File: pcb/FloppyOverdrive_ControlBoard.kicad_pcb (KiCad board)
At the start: 2 copper layers, 163 x 104 mm, 78 parts, among them IC1 THS4521IDR, IC2 THS4521IDR, IC3 MAX660MX_NOPB, J1 174804-1, J10 Flop_ADC_Header, J2 Motor_Header, J3 Floppy_Bus, J4 Sensor_Header, J5 Heads_Header, J6 Step_Header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

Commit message: Fixed pin 39, added missing hole to PCB
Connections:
- J8 pad 39: +3.3V -> +3V3
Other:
- outline, holes or cut-outs redrawn
- board text added: "+3.3V"
- board text added: "+5V"
- board text added: "2x 47uF"
- board text added: "Floppy Bus"
- board text added: "GND"
- board text added: "Replaces Mitsubishi NAMFN motherboard for MF504A"
- board text removed: "Replaces Mitsubishi NAMFN motherboard"

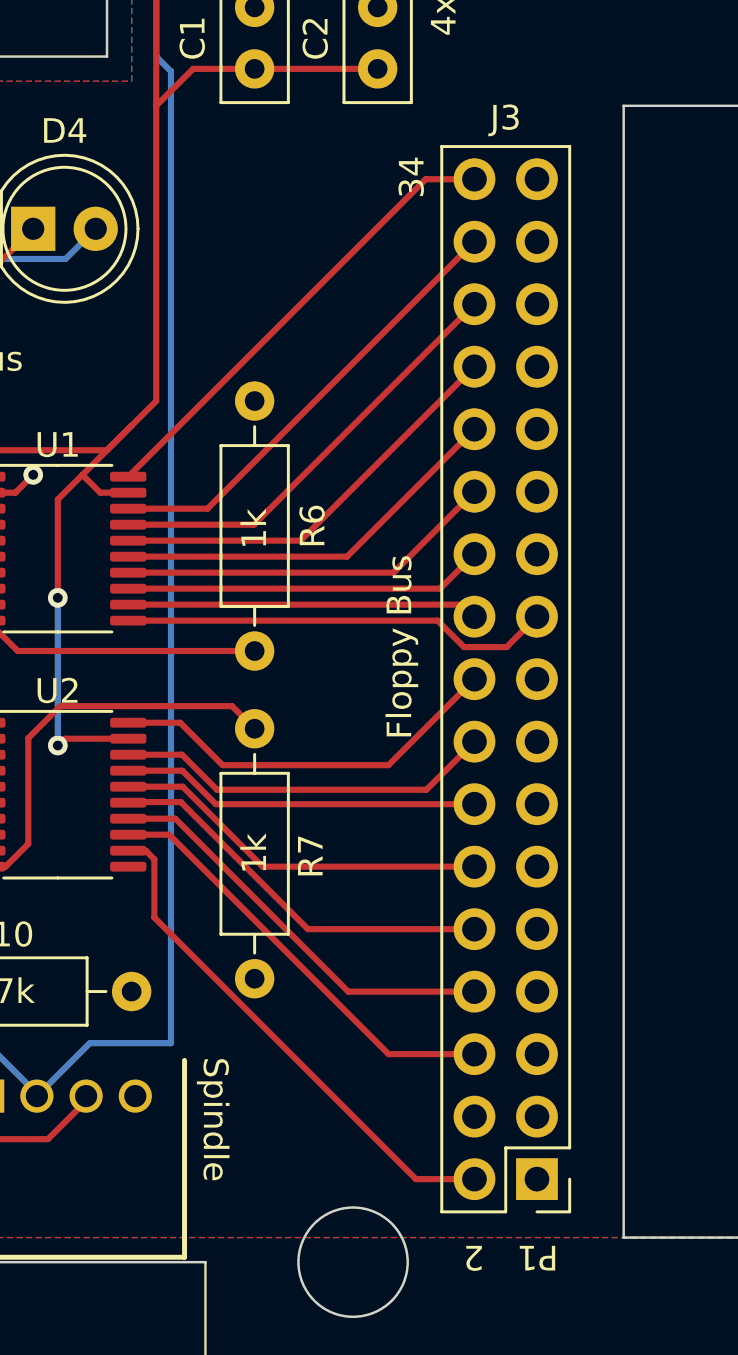
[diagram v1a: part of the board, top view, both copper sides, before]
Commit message: Added bus pinout to silkscreen
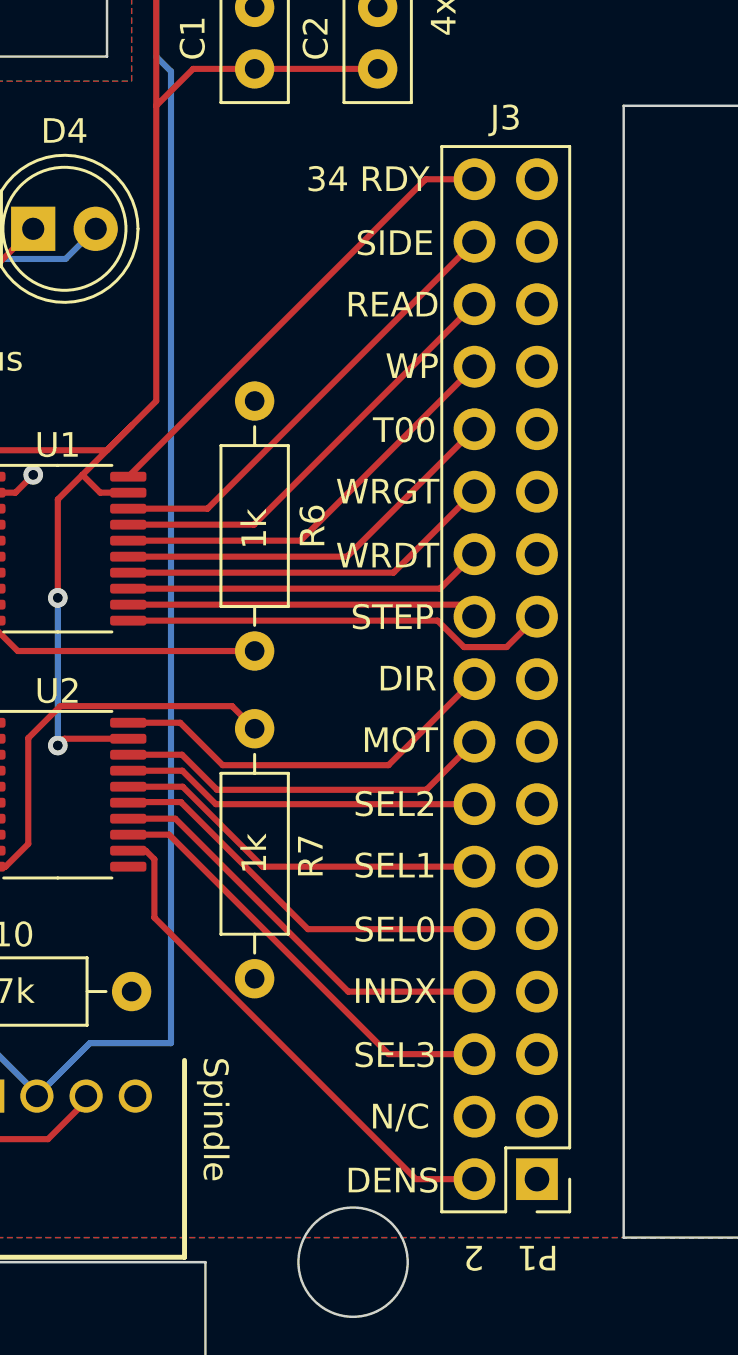
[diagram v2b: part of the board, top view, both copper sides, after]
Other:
- board text added: "34 RDY"
- board text added: "DENS"
- board text added: "DIR"
- board text added: "INDX"
- board text added: "MOT"
- board text added: "N/C"
- board text added: "READ"
- board text added: "SEL0"
- board text added: "SEL1"
- board text added: "SEL2"
- board text added: "SEL3"
- board text added: "SIDE"
- board text added: "STEP"
- board text added: "T00"
- board text added: "WRDT"
- board text added: "WRGT"
- board text removed: "34"
- board text removed: "Floppy Bus"
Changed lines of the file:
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@@
+    (effects (font (size 1 1) (thickness 0.15)))
+  )
+  (gr_text "N/C" (at 210.9 135.1) (layer "F.SilkS")
     (effects (font (size 1 1) (thickness 0.15)))
   )
@@
     (effects (font (size 1 1) (thickness 0.15)))
   )
+  (gr_text "WP" (at 211.4 104.6) (layer "F.SilkS")
+    (effects (font (size 1 1) (thickness 0.15)))
+  )
   (gr_text "Head 0      1" (at 98 98.8) (layer "F.SilkS")
     (effects (font (size 1 1) (thickness 0.15)))
   )
   (gr_text "Side A\nSide B" (at 77 118 270) (layer "F.SilkS")
+    (effects (font (size 1 1) (thickness 0.15)))
+  )
+  (gr_text "SEL1" (at 210.7 124.9) (layer "F.SilkS")
     (effects (font (size 1 1) (thickness 0.15)))
   )
@@
     (effects (font (size 0.75 0.75) (thickness 0.1)))
   )
+  (gr_text "SEL3" (at 210.7 132.6) (layer "F.SilkS")
+    (effects (font (size 1 1) (thickness 0.15)))
+  )
   (gr_text "ADC Pins" (at 154 134.2) (layer "F.SilkS")
     (effects (font (size 1 1) (thickness 0.15)))
@@
     (effects (font (size 1 1) (thickness 0.15)))
   )
+  (gr_text "INDX" (at 210.7 130) (layer "F.SilkS")
+    (effects (font (size 1 1) (thickness 0.15)))
+  )
   (gr_text "22k" (at 101.7 142.24) (layer "F.SilkS")
     (effects (font (size 1 1) (thickness 0.15)))
@@
     (effects (font (size 1 1) (thickness 0.15)))
   )
-  (gr_text "Floppy Bus" (at 210.9 116 90) (layer "F.SilkS")
+  (gr_text "DENS" (at 210.6 137.7) (layer "F.SilkS")
     (effects (font (size 1 1) (thickness 0.15)))
   )
@@
     (effects (font (size 1 1) (thickness 0.15)))
   )
+  (gr_text "MOT" (at 210.9 119.8) (layer "F.SilkS")
+    (effects (font (size 1 1) (thickness 0.15)))
+  )
+  (gr_text "WRGT" (at 210.4 109.7) (layer "F.SilkS")
+    (effects (font (size 1 1) (thickness 0.15)))
+  )
   (gr_text "ULN2003C" (at 182 121.3) (layer "F.SilkS")
     (effects (font (size 1 1) (thickness 0.15)))
   )
+  (gr_text "SIDE" (at 210.7 99.6) (layer "F.SilkS")
+    (effects (font (size 1 1) (thickness 0.15)))
+  )
+  (gr_text "READ" (at 210.6 102.1) (layer "F.SilkS")
+    (effects (font (size 1 1) (thickness 0.15)))
+  )
   (gr_text "4-Pin Power" (at 223.2 63.8 90) (layer "F.SilkS")
     (effects (font (size 1 1) (thickness 0.15)))
   )
+  (gr_text "34 RDY" (at 209.6 97) (layer "F.SilkS")
+    (effects (font (size 1 1) (thickness 0.15)))
+  )
   (gr_text "2x 33uF Electrolytic" (at 212 68 270) (layer "F.SilkS")
     (effects (font (size 1 1) (thickness 0.15)))
@@
     (effects (font (size 1 1) (thickness 0.15)))
   )
+  (gr_text "STEP" (at 210.6 114.8) (layer "F.SilkS")
+    (effects (font (size 1 1) (thickness 0.15)))
+  )
   (gr_text "0.1uF" (at 163 127.8 90) (layer "F.SilkS")
     (effects (font (size 1 1) (thickness 0.15)))
   )
+  (gr_text "SEL2" (at 210.7 122.4) (layer "F.SilkS")
+    (effects (font (size 1 1) (thickness 0.15)))
+  )
   (gr_text "+" (at 93.7 101.1) (layer "F.SilkS")
     (effects (font (size 1 1) (thickness 0.15)))
@@
     (effects (font (size 1 1) (thickness 0.15)))
   )
+  (gr_text "WRDT" (at 210.4 112.3) (layer "F.SilkS")
+    (effects (font (size 1 1) (thickness 0.15)))
+  )
+  (gr_text "SEL0" (at 210.7 127.5) (layer "F.SilkS")
+    (effects (font (size 1 1) (thickness 0.15)))
+  )
   (gr_text "510" (at 158.75 99.985 90) (layer "F.SilkS")
     (effects (font (size 1 1) (thickness 0.15)))
   )
+  (gr_text "T00" (at 211.1 107.2) (layer "F.SilkS")
+    (effects (font (size 1 1) (thickness 0.15)))
+  )
   (gr_text "1k" (at 142.75 101 90) (layer "F.SilkS")
     (effects (font (size 1 1) (thickness 0.15)))
@@
     (effects (font (size 1 1) (thickness 0.15)))
   )
+  (gr_text "DIR" (at 211.2 117.3) (layer "F.SilkS")
+    (effects (font (size 1 1) (thickness 0.15)))
+  )
   (gr_text "2x 47uF" (at 109.1 106) (layer "F.SilkS")
     (effects (font (size 1 1) (thickness 0.15)))
@@
     (effects (font (size 1 1) (thickness 0.15)))
   )
-  (gr_text "34" (at 211.4 96.9 90) (layer "F.SilkS")
-    (effects (font (size 1 1) (thickness 0.15)))
-  )

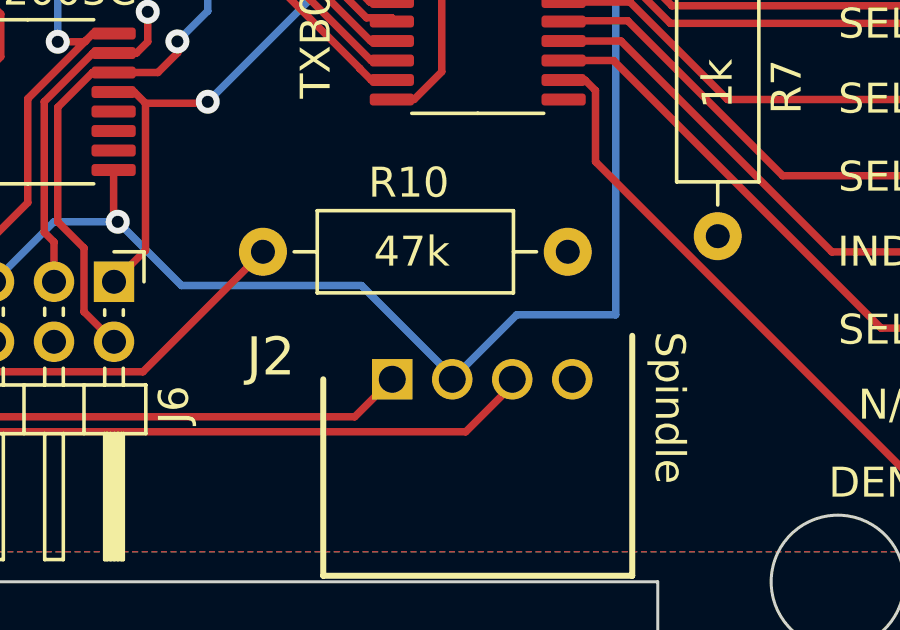
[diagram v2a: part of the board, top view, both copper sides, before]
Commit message: Added spin info to silkscreen
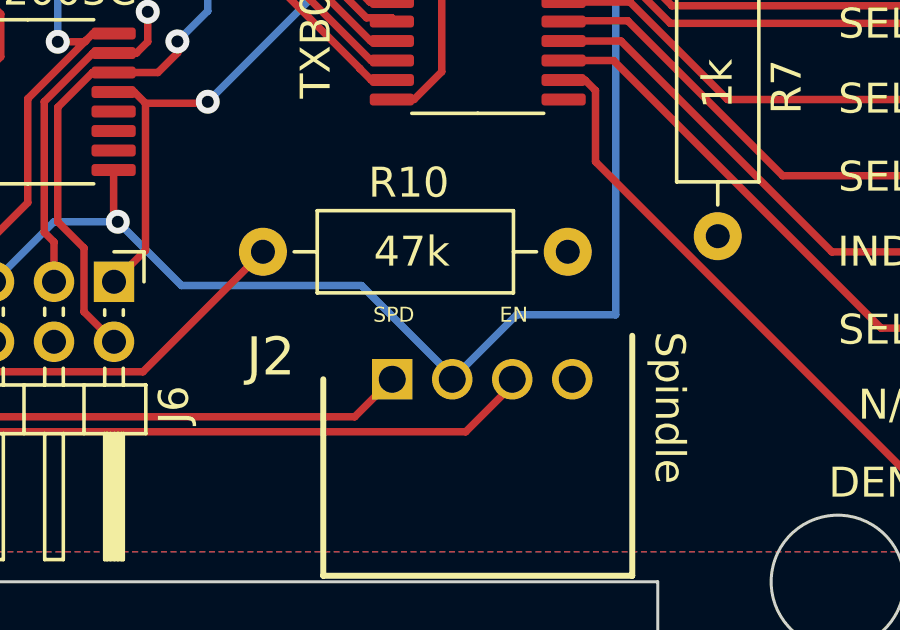
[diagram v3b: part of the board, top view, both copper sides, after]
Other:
- board text added: "EN"
- board text added: "SPD"
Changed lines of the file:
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@@
     (effects (font (size 1 1) (thickness 0.15)))
+  )
+  (gr_text "EN" (at 198.2 132.1) (layer "F.SilkS")
+    (effects (font (size 0.5 0.5) (thickness 0.125)))
   )
   (gr_text "MOT" (at 210.9 119.8) (layer "F.SilkS")
@@
     (effects (font (size 1 1) (thickness 0.15)))
   )
+  (gr_text "SPD" (at 194.2 132.1) (layer "F.SilkS")
+    (effects (font (size 0.5 0.5) (thickness 0.125)))
+  )
   (gr_text "1k" (at 205 111.2 90) (layer "F.SilkS")
